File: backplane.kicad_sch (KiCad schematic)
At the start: 7 parts, among them J16 PCB-Edge_Samtec_HSEC8_2x20_HS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, U14 ESD204DQAR, U15 ESD204DQAR, U16 ESD204DQAR

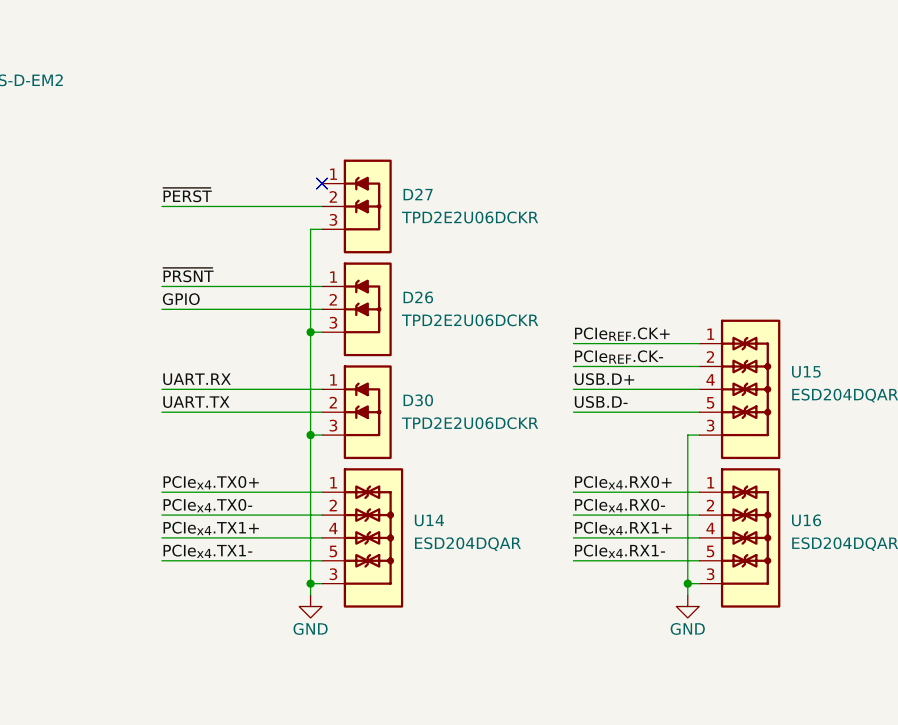
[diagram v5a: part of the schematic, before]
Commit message: [#65447] Layout PCIe, fix net names
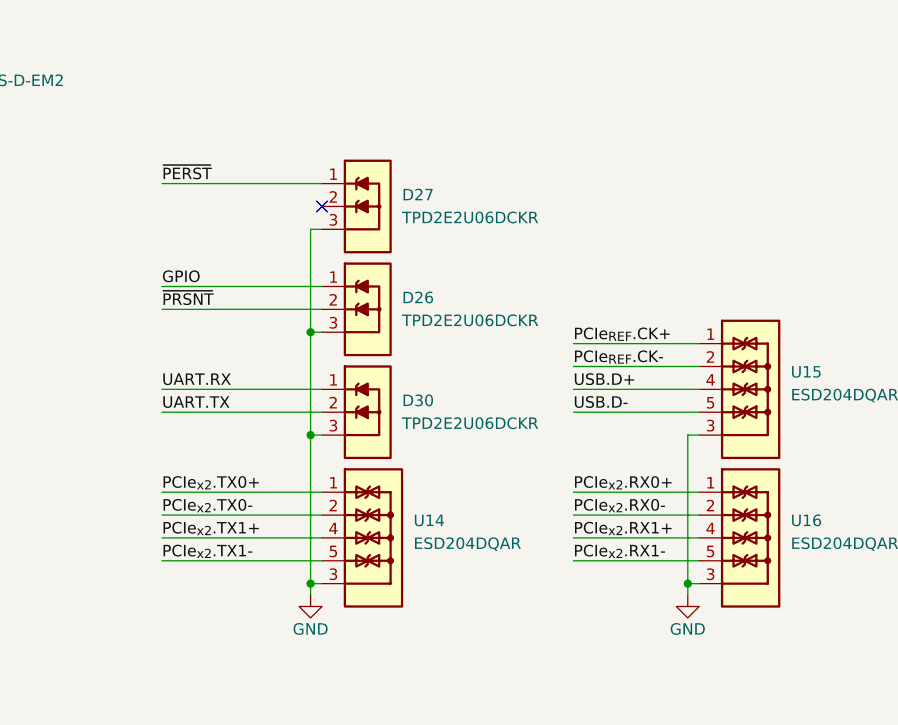
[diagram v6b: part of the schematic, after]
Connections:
- net PCIe_{x4}.RX0+ is gone; now on net PCIe_{x2}.RX0+: U16.1, U16.10
- net PCIe_{x4}.RX0- is gone; now on net PCIe_{x2}.RX0-: U16.2, U16.9
- net PCIe_{x4}.RX1+ is gone; now on net PCIe_{x2}.RX1+: U16.4, U16.7
- net PCIe_{x4}.RX1- is gone; now on net PCIe_{x2}.RX1-: U16.5, U16.6
- net PCIe_{x4}.TX0+ is gone; now on net PCIe_{x2}.TX0+: U14.1, U14.10
- net PCIe_{x4}.TX0- is gone; now on net PCIe_{x2}.TX0-: U14.2, U14.9
- net PCIe_{x4}.TX1+ is gone; now on net PCIe_{x2}.TX1+: U14.4, U14.7
- net PCIe_{x4}.TX1- is gone; now on net PCIe_{x2}.TX1-: U14.5, U14.6
- net GPIO: now also D26.1; no longer D26.2
- net ~{PERST}: now also D27.1; no longer D27.2
- net ~{PRSNT}: now also D26.2; no longer D26.1
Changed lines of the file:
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@@
   (junction (at 204.47 157.48) (diameter 0) (color 0 0 0 0)
   )
-  (no_connect (at 275.59 130.81))
+  (no_connect (at 275.59 133.35))
   (bus_entry (at 175.26 160.02) (size -1.27 1.27)
     (stroke (width 0) (type default))
@@
     (stroke (width 0) (type default))
   )
+  (wire (pts (xy 257.81 130.81) (xy 275.59 130.81))
+    (stroke (width 0) (type default))
+  )
   (wire (pts (xy 204.47 129.54) (xy 203.2 129.54))
     (stroke (width 0) (type default))
@@
     (stroke (width 0) (type default))
   )
-  (wire (pts (xy 257.81 133.35) (xy 275.59 133.35))
-    (stroke (width 0) (type default))
-  )
   (wire (pts (xy 191.77 127) (xy 190.5 127))
     (stroke (width 0) (type default))
@@
     (effects (font (size 1.27 1.27)) (justify left bottom))
   )
-  (label "PCIe_{x4}.RX0-" (at 303.53 167.64 0) (fields_autoplaced)
+  (label "PCIe_{x2}.RX0-" (at 303.53 167.64 0) (fields_autoplaced)
     (effects (font (size 1.27 1.27)) (justify left bottom))
   )
@@
     (effects (font (size 1.27 1.27)) (justify left bottom))
   )
-  (label "PCIe_{x4}.TX0+" (at 257.81 165.1 0) (fields_autoplaced)
+  (label "PCIe_{x2}.TX0+" (at 257.81 165.1 0) (fields_autoplaced)
     (effects (font (size 1.27 1.27)) (justify left bottom))
   )
@@
     (effects (font (size 1.27 1.27)) (justify left bottom))
   )
+  (label "GPIO" (at 257.81 142.24 0) (fields_autoplaced)
+    (effects (font (size 1.27 1.27)) (justify left bottom))
+  )
   (label "UART.RX" (at 205.74 167.64 0) (fields_autoplaced)
     (effects (font (size 1.27 1.27)) (justify left bottom))
@@
     (effects (font (size 1.27 1.27)) (justify right bottom))
   )
-  (label "~{PRSNT}" (at 257.81 142.24 0) (fields_autoplaced)
-    (effects (font (size 1.27 1.27)) (justify left bottom))
-  )
   (label "PCIe_{x2}.RX0+" (at 218.44 144.78 180) (fields_autoplaced)
     (effects (font (size 1.27 1.27)) (justify right bottom))
@@
     (effects (font (size 1.27 1.27)) (justify left bottom))
   )
-  (label "PCIe_{x4}.RX0+" (at 303.53 165.1 0) (fields_autoplaced)
+  (label "PCIe_{x2}.RX0+" (at 303.53 165.1 0) (fields_autoplaced)
     (effects (font (size 1.27 1.27)) (justify left bottom))
   )
@@
     (effects (font (size 1.27 1.27)) (justify right bottom))
   )
-  (label "PCIe_{x4}.RX1+" (at 303.53 170.18 0) (fields_autoplaced)
-    (effects (font (size 1.27 1.27)) (justify left bottom))
-  )
-  (label "PCIe_{x4}.TX1-" (at 257.81 172.72 0) (fields_autoplaced)
-    (effects (font (size 1.27 1.27)) (justify left bottom))
-  )
-  (label "PCIe_{x4}.TX1+" (at 257.81 170.18 0) (fields_autoplaced)
+  (label "PCIe_{x2}.RX1+" (at 303.53 170.18 0) (fields_autoplaced)
+    (effects (font (size 1.27 1.27)) (justify left bottom))
+  )
+  (label "PCIe_{x2}.TX1-" (at 257.81 172.72 0) (fields_autoplaced)
+    (effects (font (size 1.27 1.27)) (justify left bottom))
+  )
+  (label "PCIe_{x2}.TX1+" (at 257.81 170.18 0) (fields_autoplaced)
     (effects (font (size 1.27 1.27)) (justify left bottom))
   )
@@
     (effects (font (size 1.27 1.27)) (justify right bottom))
   )
-  (label "GPIO" (at 257.81 144.78 0) (fields_autoplaced)
-    (effects (font (size 1.27 1.27)) (justify left bottom))
-  )
-  (label "~{PERST}" (at 257.81 133.35 0) (fields_autoplaced)
+  (label "~{PERST}" (at 257.81 130.81 0) (fields_autoplaced)
     (effects (font (size 1.27 1.27)) (justify left bottom))
   )
@@
     (effects (font (size 1.27 1.27)) (justify left bottom))
   )
-  (label "PCIe_{x4}.RX1-" (at 303.53 172.72 0) (fields_autoplaced)
-    (effects (font (size 1.27 1.27)) (justify left bottom))
-  )
-  (label "PCIe_{x4}.TX0-" (at 257.81 167.64 0) (fields_autoplaced)
+  (label "PCIe_{x2}.RX1-" (at 303.53 172.72 0) (fields_autoplaced)
+    (effects (font (size 1.27 1.27)) (justify left bottom))
+  )
+  (label "PCIe_{x2}.TX0-" (at 257.81 167.64 0) (fields_autoplaced)
     (effects (font (size 1.27 1.27)) (justify left bottom))
   )
@@
     (effects (font (size 1.27 1.27)) (justify left bottom))
   )
+  (label "~{PRSNT}" (at 257.81 144.78 0) (fields_autoplaced)
+    (effects (font (size 1.27 1.27)) (justify left bottom))
+  )

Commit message: [#65840] Roughly route PCIe, GbE
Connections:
- net PCIe_{x2}.RX0+: now also J16.20, U16.2, U16.9; no longer J16.18, U16.1, U16.10
- net PCIe_{x2}.RX0-: now also J16.18, U16.1, U16.10; no longer J16.20, U16.2, U16.9
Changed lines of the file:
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@@
     (stroke (width 0) (type default))
   )
-  (bus_entry (at 223.52 148.59) (size -1.27 -1.27)
+  (bus_entry (at 226.06 148.59) (size -1.27 -1.27)
     (stroke (width 0) (type default))
   )
@@
     (stroke (width 0) (type default))
   )
-  (bus_entry (at 223.52 153.67) (size -1.27 -1.27)
-    (stroke (width 0) (type default))
-  )
-  (bus_entry (at 223.52 156.21) (size -1.27 -1.27)
+  (bus_entry (at 226.06 153.67) (size -1.27 -1.27)
+    (stroke (width 0) (type default))
+  )
+  (bus_entry (at 226.06 156.21) (size -1.27 -1.27)
     (stroke (width 0) (type default))
   )
@@
     (stroke (width 0) (type default))
   )
-  (bus_entry (at 223.52 146.05) (size -1.27 -1.27)
+  (bus_entry (at 226.06 146.05) (size -1.27 -1.27)
     (stroke (width 0) (type default))
   )
@@
     (stroke (width 0) (type default))
   )
-  (wire (pts (xy 203.2 147.32) (xy 222.25 147.32))
-    (stroke (width 0) (type default))
-  )
   (wire (pts (xy 190.5 157.48) (xy 191.77 157.48))
     (stroke (width 0) (type default))
   )
-  (bus (pts (xy 222.25 179.07) (xy 171.45 179.07))
-    (stroke (width 0) (type default))
-  )
-  (bus (pts (xy 223.52 146.05) (xy 223.52 148.59))
+  (bus (pts (xy 224.79 179.07) (xy 171.45 179.07))
+    (stroke (width 0) (type default))
+  )
+  (bus (pts (xy 226.06 146.05) (xy 226.06 148.59))
     (stroke (width 0) (type default))
   )
@@
     (stroke (width 0) (type default))
   )
+  (wire (pts (xy 203.2 147.32) (xy 207.01 147.32))
+    (stroke (width 0) (type default))
+  )
   (wire (pts (xy 303.53 167.64) (xy 317.5 167.64))
     (stroke (width 0) (type default))
@@
     (stroke (width 0) (type default))
   )
-  (wire (pts (xy 203.2 154.94) (xy 222.25 154.94))
-    (stroke (width 0) (type default))
-  )
   (wire (pts (xy 274.32 147.32) (xy 275.59 147.32))
     (stroke (width 0) (type default))
   )
+  (wire (pts (xy 207.01 144.78) (xy 209.55 147.32))
+    (stroke (width 0) (type default))
+  )
   (wire (pts (xy 274.32 175.26) (xy 274.32 176.53))
     (stroke (width 0) (type default))
@@
     (stroke (width 0) (type default))
   )
+  (wire (pts (xy 203.2 152.4) (xy 224.79 152.4))
+    (stroke (width 0) (type default))
+  )
   (wire (pts (xy 257.81 144.78) (xy 275.59 144.78))
     (stroke (width 0) (type default))
   )
+  (wire (pts (xy 203.2 154.94) (xy 224.79 154.94))
+    (stroke (width 0) (type default))
+  )
   (wire (pts (xy 274.32 135.89) (xy 274.32 147.32))
     (stroke (width 0) (type default))
   )
-  (wire (pts (xy 203.2 144.78) (xy 222.25 144.78))
-    (stroke (width 0) (type default))
-  )
   (wire (pts (xy 175.26 160.02) (xy 191.77 160.02))
     (stroke (width 0) (type default))
@@
     (stroke (width 0) (type default))
   )
-  (bus (pts (xy 223.52 153.67) (xy 223.52 156.21))
+  (bus (pts (xy 226.06 153.67) (xy 226.06 156.21))
     (stroke (width 0) (type default))
   )
@@
     (stroke (width 0) (type default))
   )
+  (wire (pts (xy 203.2 144.78) (xy 207.01 144.78))
+    (stroke (width 0) (type default))
+  )
   (bus (pts (xy 170.18 146.05) (xy 170.18 151.13))
     (stroke (width 0) (type default))
@@
     (stroke (width 0) (type default))
   )
-  (bus (pts (xy 223.52 177.8) (xy 222.25 179.07))
+  (bus (pts (xy 226.06 177.8) (xy 224.79 179.07))
     (stroke (width 0) (type default))
   )
@@
     (stroke (width 0) (type default))
   )
-  (wire (pts (xy 203.2 152.4) (xy 222.25 152.4))
-    (stroke (width 0) (type default))
-  )
   (wire (pts (xy 214.63 165.1) (xy 203.2 165.1))
     (stroke (width 0) (type default))
@@
     (stroke (width 0) (type default))
   )
+  (wire (pts (xy 209.55 144.78) (xy 207.01 147.32))
+    (stroke (width 0) (type default))
+  )
   (bus (pts (xy 170.18 151.13) (xy 170.18 153.67))
     (stroke (width 0) (type default))
   )
-  (bus (pts (xy 223.52 156.21) (xy 223.52 177.8))
-    (stroke (width 0) (type default))
-  )
-  (bus (pts (xy 226.06 165.1) (xy 222.25 165.1))
+  (bus (pts (xy 226.06 156.21) (xy 226.06 177.8))
+    (stroke (width 0) (type default))
+  )
+  (bus (pts (xy 229.87 165.1) (xy 222.25 165.1))
     (stroke (width 0) (type default))
   )
@@
     (stroke (width 0) (type default))
   )
+  (wire (pts (xy 209.55 147.32) (xy 224.79 147.32))
+    (stroke (width 0) (type default))
+  )
   (bus (pts (xy 171.45 179.07) (xy 170.18 177.8))
     (stroke (width 0) (type default))
   )
+  (wire (pts (xy 209.55 144.78) (xy 224.79 144.78))
+    (stroke (width 0) (type default))
+  )
   (wire (pts (xy 303.53 170.18) (xy 317.5 170.18))
     (stroke (width 0) (type default))
@@
     (stroke (width 0) (type default))
   )
-  (bus (pts (xy 223.52 148.59) (xy 223.52 153.67))
+  (bus (pts (xy 226.06 148.59) (xy 226.06 153.67))
     (stroke (width 0) (type default))
   )
@@
     (effects (font (size 1.27 1.27)) (justify left bottom))
   )
-  (label "PCIe_{x2}.RX0-" (at 303.53 167.64 0) (fields_autoplaced)
-    (effects (font (size 1.27 1.27)) (justify left bottom))
-  )
   (label "USB.D+" (at 179.07 167.64 0) (fields_autoplaced)
     (effects (font (size 1.27 1.27)) (justify left bottom))
@@
     (effects (font (size 1.27 1.27)) (justify left bottom))
   )
-  (label "PCIe_{x2}.RX1+" (at 218.44 152.4 180) (fields_autoplaced)
+  (label "PCIe_{x2}.RX1+" (at 223.52 152.4 180) (fields_autoplaced)
     (effects (font (size 1.27 1.27)) (justify right bottom))
+  )
+  (label "PCIe_{x2}.RX0-" (at 303.53 165.1 0) (fields_autoplaced)
+    (effects (font (size 1.27 1.27)) (justify left bottom))
   )
   (label "USB.D-" (at 303.53 156.21 0) (fields_autoplaced)
@@
     (effects (font (size 1.27 1.27)) (justify right bottom))
   )
-  (label "PCIe_{x2}.RX0+" (at 218.44 144.78 180) (fields_autoplaced)
+  (label "PCIe_{x2}.RX0+" (at 223.52 144.78 180) (fields_autoplaced)
     (effects (font (size 1.27 1.27)) (justify right bottom))
   )
@@
     (effects (font (size 1.27 1.27)) (justify left bottom))
   )
-  (label "PCIe_{x2}.RX0+" (at 303.53 165.1 0) (fields_autoplaced)
-    (effects (font (size 1.27 1.27)) (justify left bottom))
-  )
   (label "PCIe_{REF}.CK-" (at 303.53 151.13 0) (fields_autoplaced)
     (effects (font (size 1.27 1.27)) (justify left bottom))
@@
     (effects (font (size 1.27 1.27)) (justify left bottom))
   )
-  (label "PCIe_{x2}.RX1-" (at 218.44 154.94 180) (fields_autoplaced)
+  (label "PCIe_{x2}.RX1-" (at 223.52 154.94 180) (fields_autoplaced)
     (effects (font (size 1.27 1.27)) (justify right bottom))
   )
@@
     (effects (font (size 1.27 1.27)) (justify left bottom))
   )
-  (label "PCIe_{x2}.RX0-" (at 218.44 147.32 180) (fields_autoplaced)
+  (label "PCIe_{x2}.RX0-" (at 223.52 147.32 180) (fields_autoplaced)
     (effects (font (size 1.27 1.27)) (justify right bottom))
   )
@@
   )
   (label "USB.D+" (at 303.53 153.67 0) (fields_autoplaced)
+    (effects (font (size 1.27 1.27)) (justify left bottom))
+  )
+  (label "PCIe_{x2}.RX0+" (at 303.53 167.64 0) (fields_autoplaced)
     (effects (font (size 1.27 1.27)) (justify left bottom))
   )
@@
     (effects (font (size 1.27 1.27)) (justify left))
   )
-  (hierarchical_label "UART{UART}" (shape bidirectional) (at 226.06 165.1 0) (fields_autoplaced)
+  (hierarchical_label "UART{UART}" (shape bidirectional) (at 229.87 165.1 0) (fields_autoplaced)
     (effects (font (size 1.27 1.27)) (justify left))
   )

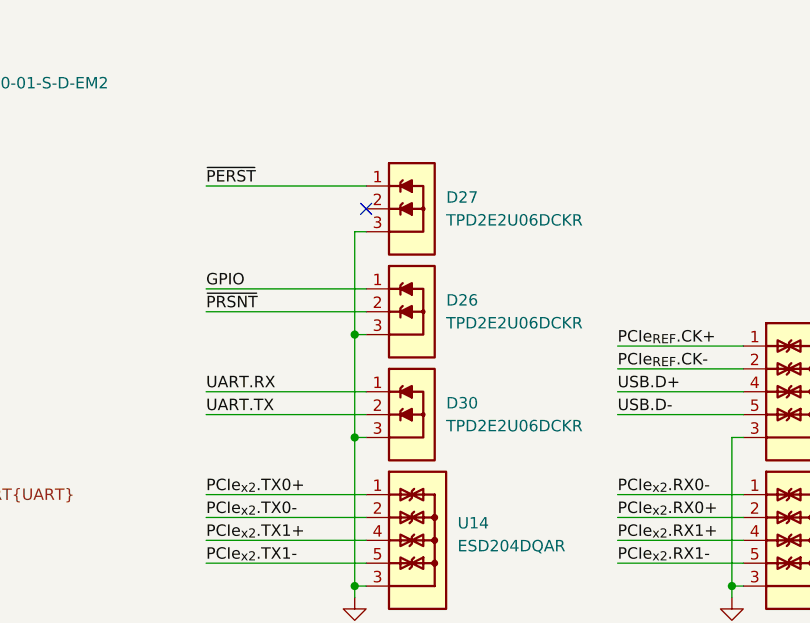
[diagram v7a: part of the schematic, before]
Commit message: [#66234] Change ESD protection diodes
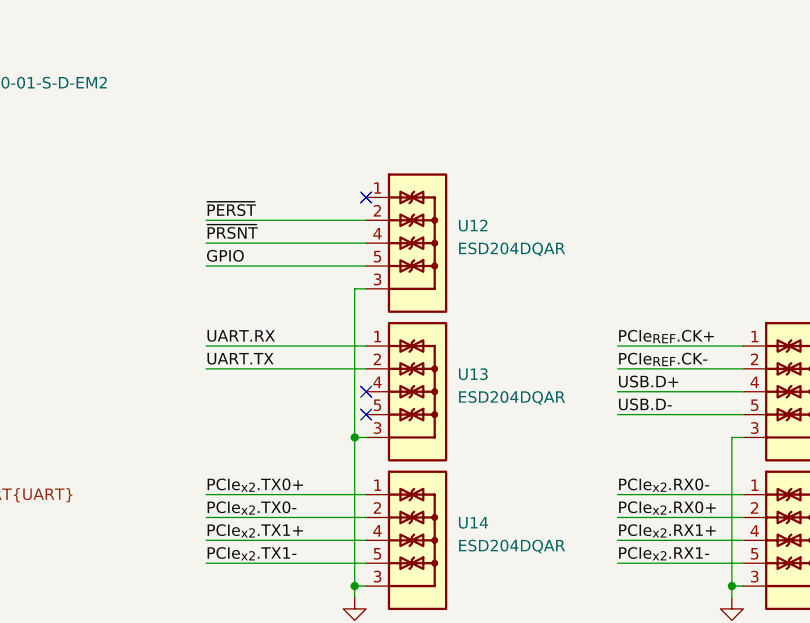
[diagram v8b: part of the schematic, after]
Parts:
- removed D26, D27, D30: TPD2E2U06_SC70, antmicro-footprints:SC70-3, symbol antmicroTVSDiodes:TPD2E2U06_SC70
- added U12, U13: ESD204DQAR, antmicro-footprints:USON-10_2.5x1mm_P0.5mm, symbol antmicroTVSDiodes:ESD204DQAR
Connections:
- net GND: now also U12.3, U12.8, U13.3, U13.8
- net GPIO: now also U12.5, U12.6
- net UART.RX: now also U13.1, U13.10
- net UART.TX: now also U13.2, U13.9
- net ~{PERST}: now also U12.2, U12.9
- net ~{PRSNT}: now also U12.4, U12.7
- new net: U13.4, U13.7
- new net: U13.5, U13.6
- new net: U12.1, U12.10
- no-connect marks 1 -> 3
